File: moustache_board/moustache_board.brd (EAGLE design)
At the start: 50 x 40 mm, 129 parts, among them CON1 B7B-PH-K-S-SIDE, CON10 PINHEAD_1X01-2.54, CON11 PINHEAD_1X01-2.54, CON12 PINHEAD_1X02-2.54, CON13 PINHEAD_1X07-2, CON14 PINHEAD_1X07-2, CON2 B7B-PH-K-S-SIDE, CON3 PINHEAD_1X02-2.54, CON4 PINHEAD_1X01-2.54, CON5 PINHEAD_1X01-2.54, CON6 PINHEAD_1X01-2.54, CON7 PINHEAD_1X01-2.54, CON8 PINHEAD_1X01-2.54, CON9 PINHEAD_1X01-2.54, IC1 STM32F030K6TX-LQFP32(7X7), IC101 IRS44273L, IC201 IRS44273L, IC3 ST3485SOIC8, IC301 IRS44273L, IC6 MC74VHC1GT125, IC7 MC74VHC1GT125, IC8 LM317, Q101 N-FET-SOT23, Q201 N-FET-SOT23, Q301 N-FET-SOT23, Y1 16MHz

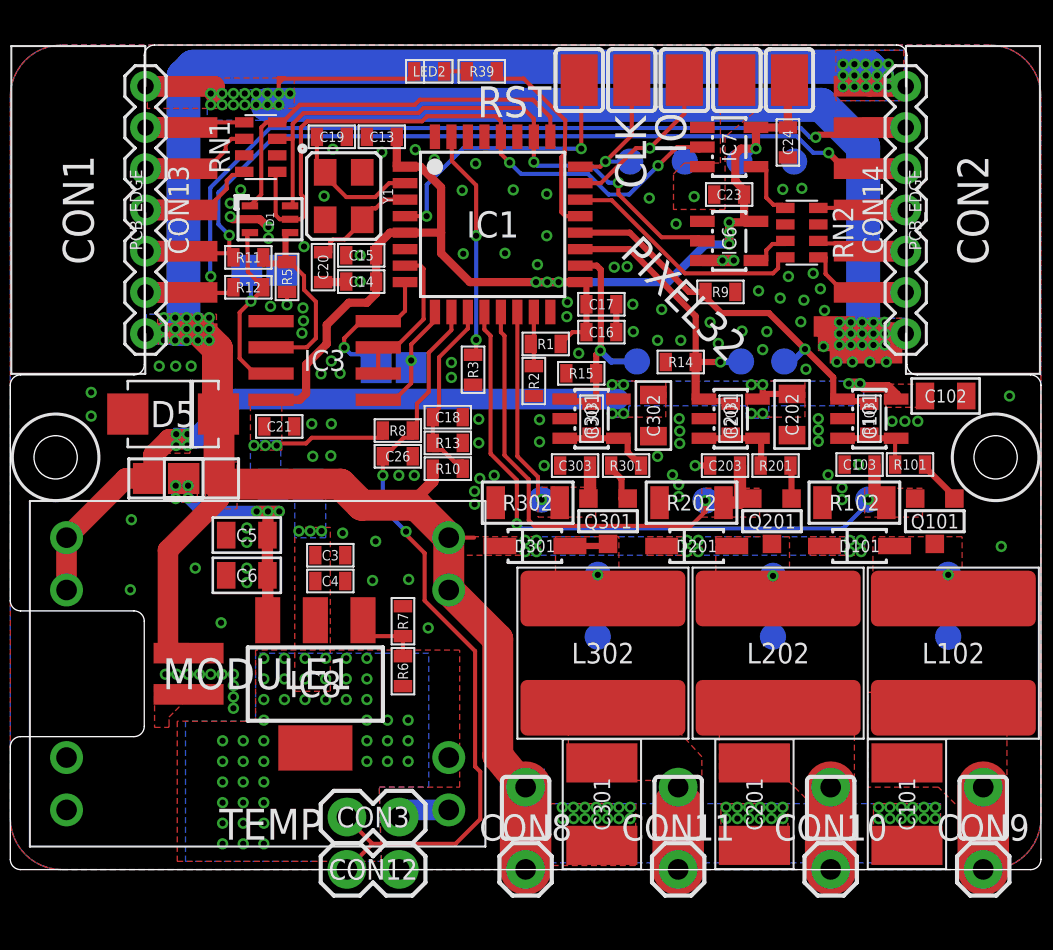
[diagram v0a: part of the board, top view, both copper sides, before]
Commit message: -directories reorganisation added gerbers for moustache board
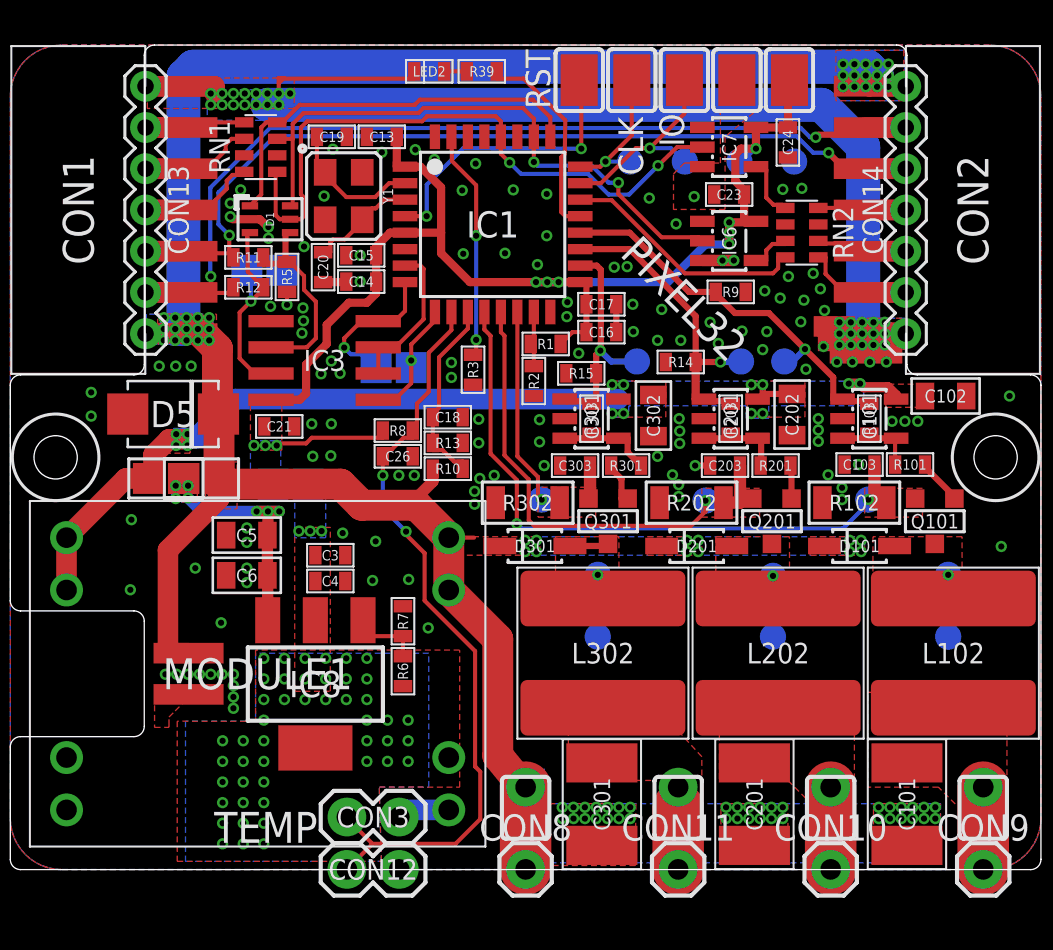
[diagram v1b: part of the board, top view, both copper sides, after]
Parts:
- moved R9 0.50 mm to (9.95, 8.03)
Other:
- board text added: "MOUSTACHE BOARD"
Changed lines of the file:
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@@
 <layer number="220" name="220bmp" color="21" fill="1" visible="no" active="no"/>
 <layer number="221" name="221bmp" color="22" fill="1" visible="no" active="no"/>
+<layer number="222" name="222bmp" color="23" fill="1" visible="no" active="no"/>
 <layer number="223" name="223bmp" color="24" fill="1" visible="no" active="no"/>
 <layer number="224" name="224bmp" color="25" fill="1" visible="no" active="no"/>
@@
 <text x="14.95" y="16.1" size="1.5" layer="22" font="vector" ratio="15" rot="MR180" align="center-right">A</text>
 <text x="14.95" y="18.1" size="1.5" layer="22" font="vector" ratio="15" rot="MR180" align="center-right">24V</text>
-<text x="-17.175" y="12.025" size="1.5" layer="22" font="vector" ratio="15" rot="MR90" align="center">IN</text>
-<text x="16.775" y="11.95" size="1.5" layer="22" font="vector" ratio="15" rot="MR90" align="center">OUT</text>
+<text x="-16.675" y="12.025" size="1.5" layer="22" font="vector" ratio="15" rot="MR90" align="center">IN</text>
+<text x="16.575" y="11.95" size="1.5" layer="22" font="vector" ratio="15" rot="MR90" align="center">OUT</text>
 <text x="-2.2" y="-15.8" size="1.5" layer="22" font="vector" ratio="15" rot="MR0" align="center">A</text>
 <text x="4.5" y="-15.6" size="1.5" layer="22" font="vector" ratio="15" rot="MR0" align="center">C1</text>
@@
 <text x="19.3" y="-15.7" size="1.5" layer="22" font="vector" ratio="15" rot="MR0" align="center">C3</text>
 <text x="5.5" y="-10.625" size="1.5" layer="22" font="vector" ratio="12" rot="MR0" align="center">j3qq4hch@gmail.com</text>
-<text x="5.1" y="14.8" size="1.5" layer="21" font="vector" ratio="15" rot="R90" align="center">CLK</text>
-<text x="7.04" y="15.725" size="1.5" layer="21" font="vector" ratio="15" rot="R90" align="center">IO</text>
+<text x="5.1" y="15.1" size="1.2" layer="21" font="vector" ratio="15" rot="R90" align="center">CLK</text>
+<text x="7.09" y="15.875" size="1.2" layer="21" font="vector" ratio="15" rot="R90" align="center">IO</text>
 <wire x1="-10.8" y1="4.8" x2="-18.2" y2="4.8" width="0.2" layer="22" style="shortdash"/>
 <wire x1="18.175" y1="4.8" x2="13.575" y2="4.8" width="0.2" layer="22" style="shortdash"/>
 <text x="-10.325" y="8.075" size="1.5" layer="22" font="vector" ratio="15" rot="MR180" align="center">T</text>
 <text x="-12.95" y="-3.125" size="1.5" layer="22" font="vector" ratio="15" rot="MR0" align="center">I measure</text>
-<text x="-12.35" y="-17.8" size="1.5" layer="21" font="vector" ratio="15" align="center">TEMP</text>
+<text x="-12.6" y="-17.95" size="1.5" layer="21" font="vector" ratio="15" align="center">TEMP</text>
 <text x="9.45" y="-12.725" size="1.5" layer="22" font="vector" ratio="12" rot="MR0" align="center">d.e.palamarchuk@gmail.com</text>
 <wire x1="14.2" y1="14.95" x2="12.35" y2="14.95" width="0.2" layer="41"/>
@@
 <wire x1="74.6" y1="-18.3" x2="67" y2="-18.3" width="0.01" layer="46"/>
 <wire x1="67" y1="-18.3" x2="67" y2="7.55" width="0.01" layer="46"/>
-<text x="-0.55" y="17.25" size="1.5" layer="21" font="vector" ratio="15" rot="R180" align="center">RST</text>
+<text x="0.6" y="18.35" size="1.2" layer="21" font="vector" ratio="15" rot="R270" align="center">RST</text>
 <text x="-55.711665625" y="-33.198" size="1.778" layer="144">LAYER-STACK</text>
 <text x="-45.932665625" y="-36.1317" size="1.778" layer="145">01-16</text>
@@
 <wire x1="-10.8" y1="10.35" x2="-10.8" y2="19.75" width="0.2" layer="22" style="shortdash"/>
 <text x="-6.4" y="2.55" size="1.3" layer="22" font="vector" ratio="15" rot="MR0" align="center">HALF DUPLEX</text>
+<text x="0" y="17.1" size="1.5" layer="30" font="vector" ratio="15" rot="MR0" align="center">MOUSTACHE BOARD</text>
 </plain>
 <attributes>
@@
 <attribute name="MANF#" value="X1E0000210013 TSX-3225 16 MHZ 9.0PF" x="-8.825" y="12.675" size="1.778" layer="27" rot="R270" display="off"/>
 </element>
-<element name="CON1" library="pixel_masterlib" package="B7B-PH-K-S_SIDE" value="B7B-PH-K-S-SIDE" x="-16.7" y="12" rot="R90">
+<element name="CON1" library="pixel_masterlib" package="B7B-PH-K-S_SIDE" value="B7B-PH-K-S-SIDE" x="-16.7" y="12" smashed="yes" rot="R90">
 <attribute name="TME#" value="B7B-PH-K-S" x="-16.7" y="12" size="1.778" layer="27" rot="R90" display="off"/>
 <attribute name="DIGIKEY#" value="455-1709-ND" x="-16.7" y="12" size="1.778" layer="27" rot="R90" display="off"/>
@@
 <attribute name="CHIPDIP#" value="9000325603" x="-16.7" y="12" size="1.778" layer="27" rot="R90" display="off"/>
 <attribute name="MANF#" value="B7B-PH-K-S(LF)(SN)" x="-16.7" y="12" size="1.778" layer="27" rot="R90" display="off"/>
+<attribute name="NAME" x="-21.7" y="12" size="1.5" layer="25" font="vector" ratio="15" rot="R90" align="center"/>
 </element>
 <element name="CON2" library="pixel_masterlib" package="B7B-PH-K-S_SIDE" value="B7B-PH-K-S-SIDE" x="16.7" y="12" rot="R270">
@@
 <attribute name="TME#" value="RC0603FR-071K6" x="-5.95" y="-7.95" size="1.778" layer="27" rot="R270" display="off"/>
 </element>
-<element name="R9" library="rc" package="R0603" value="10K" x="9.45" y="8.025" rot="R180">
-<attribute name="PACKAGE" value="0603" x="9.45" y="8.025" size="1.778" layer="27" rot="R180" display="off"/>
-<attribute name="FARNELL#" value="2008341" x="9.45" y="8.025" size="1.778" layer="27" rot="R180" display="off"/>
-<attribute name="TME#" value="RC0603FR-0710K" x="9.45" y="8.025" size="1.778" layer="27" rot="R180" display="off"/>
+<element name="R9" library="rc" package="R0603" value="10K" x="9.95" y="8.025" rot="R180">
+<attribute name="PACKAGE" value="0603" x="9.95" y="8.025" size="1.778" layer="27" rot="R180" display="off"/>
+<attribute name="FARNELL#" value="2008341" x="9.95" y="8.025" size="1.778" layer="27" rot="R180" display="off"/>
+<attribute name="TME#" value="RC0603FR-0710K" x="9.95" y="8.025" size="1.778" layer="27" rot="R180" display="off"/>
 </element>
 <element name="R14" library="rc" package="R0603" value="10K" x="7.525" y="4.625">
@@
 <via x="13.35" y="6.575" extent="1-16" drill="0.3"/>
 <via x="12.75" y="8.775" extent="1-16" drill="0.3"/>
-<via x="11.3" y="8.075" extent="1-16" drill="0.3"/>
+<via x="11.6" y="8.075" extent="1-16" drill="0.3"/>
 <via x="17.5" y="4.625" extent="1-16" drill="0.3"/>
 <via x="16.7" y="4.625" extent="1-16" drill="0.3"/>
@@
 <wire x1="15.375" y1="2.825" x2="14.925" y2="2.825" width="0.3" layer="1"/>
 <via x="13.55" y="5.25" extent="1-16" drill="0.3"/>
-<wire x1="9.5" y1="7" x2="8.725" y2="7.775" width="0.3" layer="1"/>
-<wire x1="8.725" y1="7.775" x2="8.725" y2="8.025" width="0.3" layer="1"/>
 <wire x1="5.05" y1="10.9" x2="7.925" y2="8.025" width="0.3" layer="1"/>
 <wire x1="12.55" y1="4.65" x2="12.25" y2="4.65" width="0.3" layer="16"/>
 <wire x1="12.45" y1="4.65" x2="12.55" y2="4.65" width="0.3" layer="16"/>
-<wire x1="9.5" y1="7" x2="11.8" y2="7" width="0.3" layer="1"/>
 <wire x1="12.55" y1="4.65" x2="12.95" y2="4.65" width="0.3" layer="16"/>
 <wire x1="12.95" y1="4.65" x2="13.55" y2="5.25" width="0.3" layer="16"/>
 <wire x1="11.8" y1="7" x2="13.55" y2="5.25" width="0.3" layer="1"/>
-<wire x1="7.925" y1="8.025" x2="8.725" y2="8.025" width="0.3" layer="1"/>
+<wire x1="7.925" y1="8.025" x2="9.225" y2="8.025" width="0.3" layer="1"/>
 <wire x1="13.55" y1="5.25" x2="14.925" y2="3.875" width="0.3" layer="1"/>
 <wire x1="14.925" y1="2.825" x2="14.925" y2="3.875" width="0.3" layer="1"/>
+<wire x1="11.8" y1="7" x2="10.15" y2="7" width="0.3" layer="1"/>
+<wire x1="10.15" y1="7" x2="9.325" y2="7.825" width="0.3" layer="1"/>
+<wire x1="9.325" y1="7.825" x2="9.225" y2="8.025" width="0.3" layer="1"/>
 </signal>
 <signal name="LED2_PWM">

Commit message: Minor changes
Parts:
- moved CON12 0.14 mm to (-7.54, -20.0)
- moved CON3 0.14 mm to (-7.54, -17.4)
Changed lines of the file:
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@@
 <setting verticaltext="up"/>
 </settings>
-<grid distance="0.05" unitdist="mm" unit="mm" style="lines" multiple="2" display="yes" altdistance="0.5" altunitdist="mm" altunit="mm"/>
+<grid distance="0.01" unitdist="mm" unit="mm" style="lines" multiple="1" display="yes" altdistance="0.5" altunitdist="mm" altunit="mm"/>
 <layers>
 <layer number="1" name="Top" color="4" fill="1" visible="no" active="yes"/>
@@
 <text x="-10.325" y="8.075" size="1.5" layer="22" font="vector" ratio="15" rot="MR180" align="center">T</text>
 <text x="-12.95" y="-3.125" size="1.5" layer="22" font="vector" ratio="15" rot="MR0" align="center">I measure</text>
-<text x="-12.6" y="-17.95" size="1.5" layer="21" font="vector" ratio="15" align="center">TEMP</text>
+<text x="-12.79" y="-17.95" size="1.5" layer="21" font="vector" ratio="15" align="center">TEMP</text>
 <text x="9.45" y="-12.725" size="1.5" layer="22" font="vector" ratio="12" rot="MR0" align="center">d.e.palamarchuk@gmail.com</text>
 <wire x1="14.2" y1="14.95" x2="12.35" y2="14.95" width="0.2" layer="41"/>
@@
 <attribute name="TME#" value="RC0603FR-0710K" x="-6.2" y="1.3" size="1.778" layer="27" rot="R180" display="off"/>
 </element>
-<element name="CON3" library="pinhead" package="1X02-PTH-2.54" value="PINHEAD_1X02-2.54" x="-7.4" y="-17.45" rot="R180"/>
+<element name="CON3" library="pinhead" package="1X02-PTH-2.54" value="PINHEAD_1X02-2.54" x="-7.54" y="-17.45" rot="R180"/>
 <element name="C26" library="rc" package="C0603" value="100 nF" x="-6.2" y="0.05" rot="R180">
 <attribute name="PACKAGE" value="0603" x="-6.2" y="0.05" size="1.778" layer="27" rot="R180" display="off"/>
@@
 <element name="CON10" library="pinhead" package="1X01-PTH-2.54" value="PINHEAD_1X01-2.54" x="14.8" y="-19.99"/>
 <element name="CON11" library="pinhead" package="1X01-PTH-2.54" value="PINHEAD_1X01-2.54" x="7.4" y="-19.99"/>
-<element name="CON12" library="pinhead" package="1X02-PTH-2.54" value="PINHEAD_1X02-2.54" x="-7.4" y="-19.99" rot="R180"/>
+<element name="CON12" library="pinhead" package="1X02-PTH-2.54" value="PINHEAD_1X02-2.54" x="-7.54" y="-19.99" rot="R180"/>
 <element name="D5" library="pixel_masterlib" package="SMB" value="TVS_DIODE-SMB" x="-17.1" y="2.1">
 <attribute name="CHIPDIP#" value="8023193826" x="-17.1" y="2.1" size="1.778" layer="27" display="off"/>
@@
 <vertex x="-16.6" y="-11.9"/>
 </polygon>
-<wire x1="-6.13" y1="-17.45" x2="-5.784" y2="-17.104" width="1" layer="16"/>
+<wire x1="-6.27" y1="-17.45" x2="-5.784" y2="-17.104" width="1" layer="16"/>
 <wire x1="-5.784" y1="-17.104" x2="-3.729" y2="-17.104" width="1" layer="16"/>
 </signal>
@@
 <wire x1="-4.7" y1="3.175" x2="-4.7" y2="5.075" width="0.2" layer="1"/>
 <wire x1="-4.7" y1="5.075" x2="-3.6" y2="6.175" width="0.2" layer="1"/>
-<wire x1="-8.67" y1="-19.99" x2="-7.43" y2="-18.75" width="0.2" layer="1"/>
-<wire x1="-7.43" y1="-18.75" x2="-3.4" y2="-18.75" width="0.2" layer="1"/>
+<wire x1="-8.81" y1="-19.99" x2="-7.57" y2="-18.75" width="0.2" layer="1"/>
+<wire x1="-7.57" y1="-18.75" x2="-3.4" y2="-18.75" width="0.2" layer="1"/>
 <wire x1="-3.4" y1="-18.75" x2="-2.2" y2="-17.55" width="0.2" layer="1"/>
 <wire x1="-2.2" y1="-17.55" x2="-2.2" y2="-15.25" width="0.2" layer="1"/>
@@
 <wire x1="-6.925" y1="-0.875" x2="-6.925" y2="-2.475" width="0.2" layer="16"/>
 <wire x1="-6.925" y1="-2.475" x2="-5.8" y2="-3.6" width="0.2" layer="16"/>
-<wire x1="-7.43" y1="-18.75" x2="-8.67" y2="-17.51" width="0.2" layer="1"/>
-<wire x1="-8.67" y1="-17.51" x2="-8.67" y2="-17.45" width="0.2" layer="1"/>
+<wire x1="-7.57" y1="-18.75" x2="-8.81" y2="-17.51" width="0.2" layer="1"/>
+<wire x1="-8.81" y1="-17.51" x2="-8.81" y2="-17.45" width="0.2" layer="1"/>
 </signal>
 <signal name="LED1_PWM">
@@
 <polygon width="0.2" layer="1" thermals="no">
 <vertex x="-16.9" y="-19.6"/>
-<vertex x="-7" y="-19.6"/>
+<vertex x="-7.14" y="-19.6"/>
 <vertex x="-7.1" y="-16"/>
 <vertex x="-3.2" y="-16"/>
@@
 <polygon width="0.2" layer="16" thermals="no">
 <vertex x="-16.5" y="-19.6"/>
-<vertex x="-7" y="-19.6"/>
+<vertex x="-7.14" y="-19.6"/>
 <vertex x="-7.1" y="-16"/>
 <vertex x="-4.7" y="-16"/>
